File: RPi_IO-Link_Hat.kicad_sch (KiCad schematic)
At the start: 45 parts, among them J1 Jack-DC, J2 Raspberry_Pi_2_3, J3 Conn_01x03_Male, J4 Conn_01x03_Male, J5 Conn_01x03_Male, J6 Conn_01x03_Male, Q1 Q_PMOS_GSD, Q2 Q_NMOS_GSD, Q3 Q_NMOS_GSD, Q4 FQT7N10LTF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

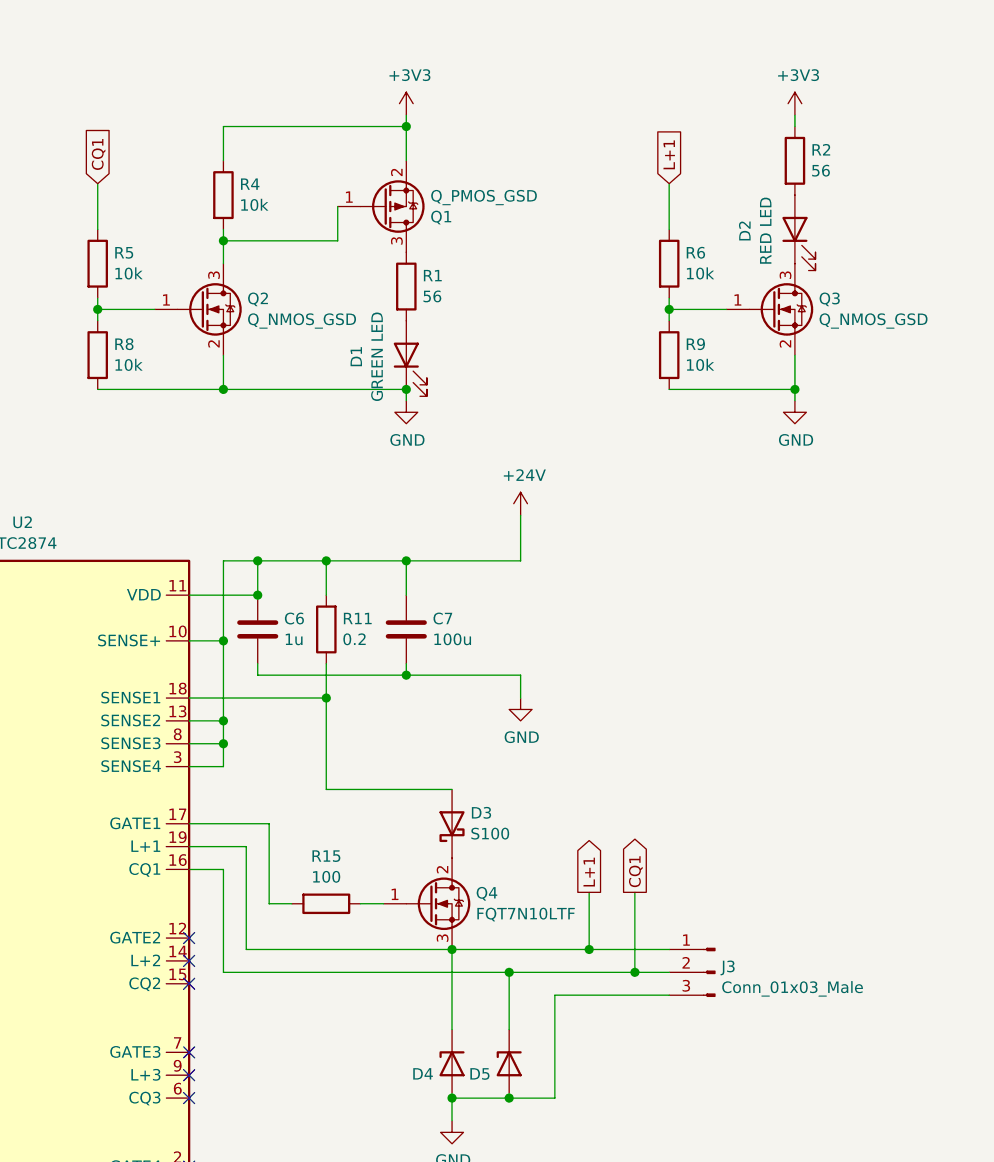
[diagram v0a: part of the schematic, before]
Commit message: fix: 改善 - CQ H で LED を点灯させるようにした - TP を追加
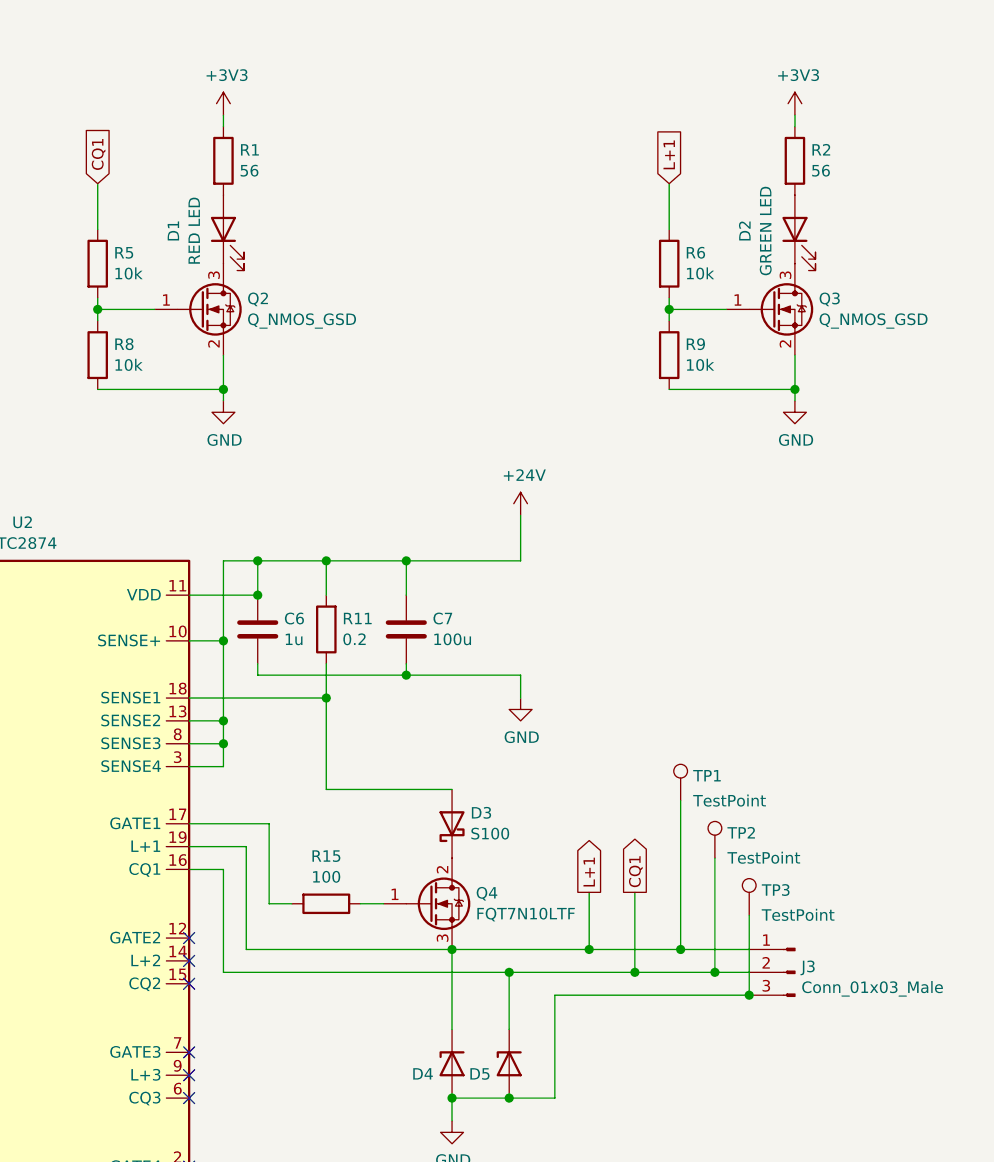
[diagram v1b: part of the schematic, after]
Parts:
- removed Q1: Q_PMOS_GSD, Package_TO_SOT_SMD:SOT-23, symbol Device:Q_PMOS_GSD
- removed R4: 10k, Resistor_SMD:R_0805_2012Metric_Pad1.20x1.40mm_HandSolder, symbol Device:R
- added TP1, TP2, TP3: TestPoint, TestPoint:TestPoint_Loop_D1.80mm_Drill1.0mm_Beaded, symbol Connector:TestPoint
- C7: footprint Capacitor_THT:CP_Radial_D10.0mm_P7.50mm -> Capacitor_THT:CP_Radial_D8.0mm_P3.50mm
- D1: value GREEN LED -> RED LED
- D2: value RED LED -> GREEN LED
- Q4: footprint Package_TO_SOT_SMD:SOT-223-3_TabPin2 -> Local:SOT-223-3_TabPin2_empty
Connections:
- net +3V3: now also R1.1
- net CQ1: now also TP2.1
- net GND: now also TP3.1; no longer D1.1 (K)
- net L+1: now also TP1.1
- net at Q2.3 (D): now also D1.1 (K)
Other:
- moved on the sheet: D1, J3, R1
